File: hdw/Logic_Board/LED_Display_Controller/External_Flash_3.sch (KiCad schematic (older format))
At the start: 16 parts, among them U2001 SST25PF020B

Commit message: Added some digikey partnumbers to components
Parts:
- C2001: footprint (none) -> Capacitors_SMD:C_0603; Digi-Key PN PN -> 311-1344-1-ND; Voltage 25V -> 50V
- C2002: Digi-Key PN PN -> 1276-1921-1-ND; Voltage 25V -> 50V
- C2003: Digi-Key PN PN -> 1276-1018-1-ND; Voltage 25V -> 50V
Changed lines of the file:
@@
 F 0 "C2001" H 5815 5530 50  0000 L CNN
 F 1 "0.1uF" H 5815 5330 50  0000 L CNN
-F 2 "" H 5828 5280 50  0001 C CNN
+F 2 "Capacitors_SMD:C_0603" H 5828 5280 50  0001 C CNN
 F 3 "" H 5815 5530 50  0001 C CNN
 F 4 "0603" H 5640 5530 50  0000 R CNN "display_footprint"
-F 5 "25V" H 5640 5430 50  0000 R CNN "Voltage"
+F 5 "50V" H 5640 5430 50  0000 R CNN "Voltage"
 F 6 "X7R" H 5640 5330 50  0000 R CNN "Dielectric"
-F 7 "PN" H 6215 5930 60  0001 C CNN "Digi-Key PN"
+F 7 "311-1344-1-ND" H 6215 5930 60  0001 C CNN "Digi-Key PN"
 	1    5790 5430
 	1    0    0    -1
@@
 F 3 "" H 6115 5530 50  0001 C CNN
 F 4 "0603" H 5940 5530 50  0001 R CNN "display_footprint"
-F 5 "25V" H 5940 5430 50  0001 R CNN "Voltage"
+F 5 "50V" H 5940 5430 50  0001 R CNN "Voltage"
 F 6 "X7R" H 5940 5330 50  0001 R CNN "Dielectric"
-F 7 "PN" H 6515 5930 60  0001 C CNN "Digi-Key PN"
+F 7 "1276-1921-1-ND" H 6515 5930 60  0001 C CNN "Digi-Key PN"
 	1    6090 5430
 	1    0    0    -1
@@
 F 3 "" H 6415 5530 50  0001 C CNN
 F 4 "0603" H 6240 5530 50  0001 R CNN "display_footprint"
-F 5 "25V" H 6240 5430 50  0001 R CNN "Voltage"
+F 5 "50V" H 6240 5430 50  0001 R CNN "Voltage"
 F 6 "X7R" H 6240 5330 50  0001 R CNN "Dielectric"
-F 7 "PN" H 6815 5930 60  0001 C CNN "Digi-Key PN"
+F 7 "1276-1018-1-ND" H 6815 5930 60  0001 C CNN "Digi-Key PN"
 	1    6390 5430
 	1    0    0    -1

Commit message: Finished first pass of digikey part numbers
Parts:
- R2001, R2002, R2003, R2004, R2005, R2012: Digi-Key PN PN -> A106047CT-ND
- R2006, R2007, R2008, R2009, R2010, R2011: Digi-Key PN PN -> RMCF0603FT10K0CT-ND
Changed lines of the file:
@@
 F 5 "1%" H 5410 4320 50  0000 L CNN "Tolerance"
 F 6 "1/10W" H 5410 4240 50  0000 L CNN "Wattage"
-F 7 "PN" H 5630 4720 60  0001 C CNN "Digi-Key PN"
+F 7 "RMCF0603FT10K0CT-ND" H 5630 4720 60  0001 C CNN "Digi-Key PN"
 	1    5330 4320
 	1    0    0    -1
@@
 F 5 "1%" H 4600 4320 50  0000 L CNN "Tolerance"
 F 6 "1/10W" H 4600 4240 50  0000 L CNN "Wattage"
-F 7 "PN" H 4820 4720 60  0001 C CNN "Digi-Key PN"
+F 7 "RMCF0603FT10K0CT-ND" H 4820 4720 60  0001 C CNN "Digi-Key PN"
 	1    4520 4320
 	1    0    0    -1
@@
 F 5 "1%" H 5190 3130 50  0000 L CNN "Tolerance"
 F 6 "1/10W" H 5190 3050 50  0000 L CNN "Wattage"
-F 7 "PN" H 5410 3530 60  0001 C CNN "Digi-Key PN"
+F 7 "RMCF0603FT10K0CT-ND" H 5410 3530 60  0001 C CNN "Digi-Key PN"
 	1    5110 3130
 	1    0    0    -1
@@
 F 5 "1%" H 4600 3130 50  0000 L CNN "Tolerance"
 F 6 "1/10W" H 4600 3050 50  0000 L CNN "Wattage"
-F 7 "PN" H 4820 3530 60  0001 C CNN "Digi-Key PN"
+F 7 "RMCF0603FT10K0CT-ND" H 4820 3530 60  0001 C CNN "Digi-Key PN"
 	1    4520 3130
 	1    0    0    -1
@@
 F 5 "1%" H 4010 3130 50  0000 L CNN "Tolerance"
 F 6 "1/10W" H 4010 3050 50  0000 L CNN "Wattage"
-F 7 "PN" H 4230 3530 60  0001 C CNN "Digi-Key PN"
+F 7 "RMCF0603FT10K0CT-ND" H 4230 3530 60  0001 C CNN "Digi-Key PN"
 	1    3930 3130
 	1    0    0    -1
@@
 F 5 "1%" H 6830 3850 50  0000 L CNN "Tolerance"
 F 6 "1/10W" H 6830 3770 50  0000 L CNN "Wattage"
-F 7 "PN" H 7050 4250 60  0001 C CNN "Digi-Key PN"
+F 7 "RMCF0603FT10K0CT-ND" H 7050 4250 60  0001 C CNN "Digi-Key PN"
 	1    6750 3850
 	1    0    0    -1
@@
 F 5 "1%" V 3620 3450 50  0001 C CNN "Tolerance"
 F 6 "1/10W" V 3720 3450 50  0001 C CNN "Wattage"
-F 7 "PN" H 3720 3850 60  0001 C CNN "Digi-Key PN"
+F 7 "A106047CT-ND" H 3720 3850 60  0001 C CNN "Digi-Key PN"
 	1    3420 3450
 	0    1    1    0
@@
 F 5 "1%" V 7330 3450 50  0001 C CNN "Tolerance"
 F 6 "1/10W" V 7430 3450 50  0001 C CNN "Wattage"
-F 7 "PN" H 7430 3850 60  0001 C CNN "Digi-Key PN"
+F 7 "A106047CT-ND" H 7430 3850 60  0001 C CNN "Digi-Key PN"
 	1    7130 3450
 	0    1    1    0
@@
 F 5 "1%" V 3620 3550 50  0001 C CNN "Tolerance"
 F 6 "1/10W" V 3720 3550 50  0001 C CNN "Wattage"
-F 7 "PN" H 3720 3950 60  0001 C CNN "Digi-Key PN"
+F 7 "A106047CT-ND" H 3720 3950 60  0001 C CNN "Digi-Key PN"
 	1    3420 3550
 	0    1    1    0
@@
 F 5 "1%" V 3620 3750 50  0001 C CNN "Tolerance"
 F 6 "1/10W" V 3720 3750 50  0001 C CNN "Wattage"
-F 7 "PN" H 3720 4150 60  0001 C CNN "Digi-Key PN"
+F 7 "A106047CT-ND" H 3720 4150 60  0001 C CNN "Digi-Key PN"
 	1    3420 3750
 	0    1    1    0
@@
 F 5 "1%" V 3620 3850 50  0001 C CNN "Tolerance"
 F 6 "1/10W" V 3720 3850 50  0001 C CNN "Wattage"
-F 7 "PN" H 3720 4250 60  0001 C CNN "Digi-Key PN"
+F 7 "A106047CT-ND" H 3720 4250 60  0001 C CNN "Digi-Key PN"
 	1    3420 3850
 	0    1    1    0
@@
 F 5 "1%" V 3620 3650 50  0001 C CNN "Tolerance"
 F 6 "1/10W" V 3720 3650 50  0001 C CNN "Wattage"
-F 7 "PN" H 3720 4050 60  0001 C CNN "Digi-Key PN"
+F 7 "A106047CT-ND" H 3720 4050 60  0001 C CNN "Digi-Key PN"
 	1    3420 3650
 	0    1    1    0

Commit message: First pass assignment of footprints to all components
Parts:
- C2002, C2003: footprint (none) -> Capacitors_SMD:C_0603
- R2001, R2002, R2003, R2004, R2005, R2006, R2007, R2008, R2009, R2010, R2011, R2012: footprint (none) -> Resistors_SMD:R_0603
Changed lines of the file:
@@
 F 0 "R2010" H 5270 4320 50  0000 R CNN
 F 1 "10k" V 5330 4320 50  0000 C CNN
-F 2 "" H 5330 4320 50  0001 C CNN
+F 2 "Resistors_SMD:R_0603" H 5330 4320 50  0001 C CNN
 F 3 "" H 5330 4320 50  0001 C CNN
 F 4 "0603" H 5410 4400 50  0000 L CNN "display_footprint"
@@
 F 0 "R2008" H 4460 4320 50  0000 R CNN
 F 1 "10k" V 4520 4320 50  0000 C CNN
-F 2 "" H 4520 4320 50  0001 C CNN
+F 2 "Resistors_SMD:R_0603" H 4520 4320 50  0001 C CNN
 F 3 "" H 4520 4320 50  0001 C CNN
 F 4 "0603" H 4600 4400 50  0000 L CNN "display_footprint"
@@
 F 0 "R2009" H 5050 3130 50  0000 R CNN
 F 1 "10k" V 5110 3130 50  0000 C CNN
-F 2 "" H 5110 3130 50  0001 C CNN
+F 2 "Resistors_SMD:R_0603" H 5110 3130 50  0001 C CNN
 F 3 "" H 5110 3130 50  0001 C CNN
 F 4 "0603" H 5190 3210 50  0000 L CNN "display_footprint"
@@
 F 0 "R2007" H 4460 3130 50  0000 R CNN
 F 1 "10k" V 4520 3130 50  0000 C CNN
-F 2 "" H 4520 3130 50  0001 C CNN
+F 2 "Resistors_SMD:R_0603" H 4520 3130 50  0001 C CNN
 F 3 "" H 4520 3130 50  0001 C CNN
 F 4 "0603" H 4600 3210 50  0000 L CNN "display_footprint"
@@
 F 0 "R2006" H 3870 3130 50  0000 R CNN
 F 1 "10k" V 3930 3130 50  0000 C CNN
-F 2 "" H 3930 3130 50  0001 C CNN
+F 2 "Resistors_SMD:R_0603" H 3930 3130 50  0001 C CNN
 F 3 "" H 3930 3130 50  0001 C CNN
 F 4 "0603" H 4010 3210 50  0000 L CNN "display_footprint"
@@
 F 0 "R2011" H 6690 3850 50  0000 R CNN
 F 1 "10k" V 6750 3850 50  0000 C CNN
-F 2 "" H 6750 3850 50  0001 C CNN
+F 2 "Resistors_SMD:R_0603" H 6750 3850 50  0001 C CNN
 F 3 "" H 6750 3850 50  0001 C CNN
 F 4 "0603" H 6830 3930 50  0000 L CNN "display_footprint"
@@
 F 0 "R2001" V 3380 3580 50  0000 L CNN
 F 1 "100" V 3420 3450 50  0000 C CNN
-F 2 "" H 3420 3450 50  0001 C CNN
+F 2 "Resistors_SMD:R_0603" H 3420 3450 50  0001 C CNN
 F 3 "" H 3420 3450 50  0001 C CNN
 F 4 "0603" V 3520 3450 50  0001 C CNN "display_footprint"
@@
 F 0 "R2012" V 7030 3450 50  0000 C CNN
 F 1 "100" V 7130 3450 50  0000 C CNN
-F 2 "" H 7130 3450 50  0001 C CNN
+F 2 "Resistors_SMD:R_0603" H 7130 3450 50  0001 C CNN
 F 3 "" H 7130 3450 50  0001 C CNN
 F 4 "0603" V 7230 3450 50  0001 C CNN "display_footprint"
@@
 F 0 "C2002" H 6115 5530 50  0000 L CNN
 F 1 "10nF" H 6115 5330 50  0000 L CNN
-F 2 "" H 6128 5280 50  0001 C CNN
+F 2 "Capacitors_SMD:C_0603" H 6128 5280 50  0001 C CNN
 F 3 "" H 6115 5530 50  0001 C CNN
 F 4 "0603" H 5940 5530 50  0001 R CNN "display_footprint"
@@
 F 0 "C2003" H 6415 5530 50  0000 L CNN
 F 1 "1nF" H 6415 5330 50  0000 L CNN
-F 2 "" H 6428 5280 50  0001 C CNN
+F 2 "Capacitors_SMD:C_0603" H 6428 5280 50  0001 C CNN
 F 3 "" H 6415 5530 50  0001 C CNN
 F 4 "0603" H 6240 5530 50  0001 R CNN "display_footprint"
@@
 F 0 "R2002" V 3380 3680 50  0000 L CNN
 F 1 "100" V 3420 3550 50  0000 C CNN
-F 2 "" H 3420 3550 50  0001 C CNN
+F 2 "Resistors_SMD:R_0603" H 3420 3550 50  0001 C CNN
 F 3 "" H 3420 3550 50  0001 C CNN
 F 4 "0603" V 3520 3550 50  0001 C CNN "display_footprint"
@@
 F 0 "R2004" V 3380 3880 50  0000 L CNN
 F 1 "100" V 3420 3750 50  0000 C CNN
-F 2 "" H 3420 3750 50  0001 C CNN
+F 2 "Resistors_SMD:R_0603" H 3420 3750 50  0001 C CNN
 F 3 "" H 3420 3750 50  0001 C CNN
 F 4 "0603" V 3520 3750 50  0001 C CNN "display_footprint"
@@
 F 0 "R2005" V 3380 3980 50  0000 L CNN
 F 1 "100" V 3420 3850 50  0000 C CNN
-F 2 "" H 3420 3850 50  0001 C CNN
+F 2 "Resistors_SMD:R_0603" H 3420 3850 50  0001 C CNN
 F 3 "" H 3420 3850 50  0001 C CNN
 F 4 "0603" V 3520 3850 50  0001 C CNN "display_footprint"
@@
 F 0 "R2003" V 3380 3780 50  0000 L CNN
 F 1 "100" V 3420 3650 50  0000 C CNN
-F 2 "" H 3420 3650 50  0001 C CNN
+F 2 "Resistors_SMD:R_0603" H 3420 3650 50  0001 C CNN
 F 3 "" H 3420 3650 50  0001 C CNN
 F 4 "0603" V 3520 3650 50  0001 C CNN "display_footprint"

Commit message: Resolved a few library dependencies
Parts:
- R2001, R2002, R2003, R2004, R2005, R2006, R2007, R2008, R2009, R2010, R2011, R2012: symbol Custom_Library:R_Custom -> LED_Display_Local_Library:R_Custom
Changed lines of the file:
@@
 $EndComp
 $Comp
-L Custom_Library:R_Custom R2010
+L LED_Display_Local_Library:R_Custom R2010
 U 1 1 5BBE8125
 P 5330 4320
@@
 $EndComp
 $Comp
-L Custom_Library:R_Custom R2008
+L LED_Display_Local_Library:R_Custom R2008
 U 1 1 5BBE8130
 P 4520 4320
@@
 $EndComp
 $Comp
-L Custom_Library:R_Custom R2009
+L LED_Display_Local_Library:R_Custom R2009
 U 1 1 5BBE813B
 P 5110 3130
@@
 $EndComp
 $Comp
-L Custom_Library:R_Custom R2007
+L LED_Display_Local_Library:R_Custom R2007
 U 1 1 5BBE8146
 P 4520 3130
@@
 $EndComp
 $Comp
-L Custom_Library:R_Custom R2006
+L LED_Display_Local_Library:R_Custom R2006
 U 1 1 5BBE8151
 P 3930 3130
@@
 $EndComp
 $Comp
-L Custom_Library:R_Custom R2011
+L LED_Display_Local_Library:R_Custom R2011
 U 1 1 5BBE815C
 P 6750 3850
@@
 $EndComp
 $Comp
-L Custom_Library:R_Custom R2001
+L LED_Display_Local_Library:R_Custom R2001
 U 1 1 5BBE818B
 P 3420 3450
@@
 FLASH_SCK
 $Comp
-L Custom_Library:R_Custom R2012
+L LED_Display_Local_Library:R_Custom R2012
 U 1 1 5BBE81B8
 P 7130 3450
@@
 	6090 5240 6390 5240
 $Comp
-L Custom_Library:R_Custom R2002
+L LED_Display_Local_Library:R_Custom R2002
 U 1 1 5BBE8203
 P 3420 3550
@@
 $EndComp
 $Comp
-L Custom_Library:R_Custom R2004
+L LED_Display_Local_Library:R_Custom R2004
 U 1 1 5BBE820E
 P 3420 3750
@@
 $EndComp
 $Comp
-L Custom_Library:R_Custom R2005
+L LED_Display_Local_Library:R_Custom R2005
 U 1 1 5BBE8219
 P 3420 3850
@@
 ~FLASH_Hold
 $Comp
-L Custom_Library:R_Custom R2003
+L LED_Display_Local_Library:R_Custom R2003
 U 1 1 5BC1CF11
 P 3420 3650

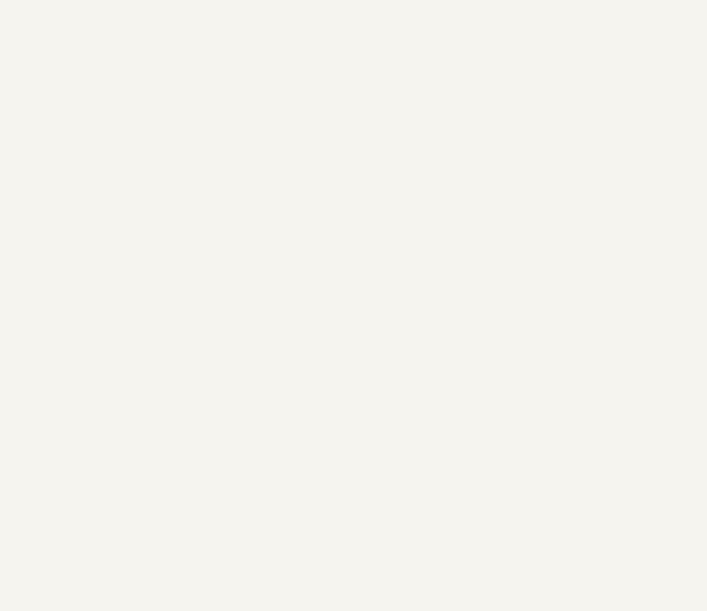
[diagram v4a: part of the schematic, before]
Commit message: Added flash chip select LEDs
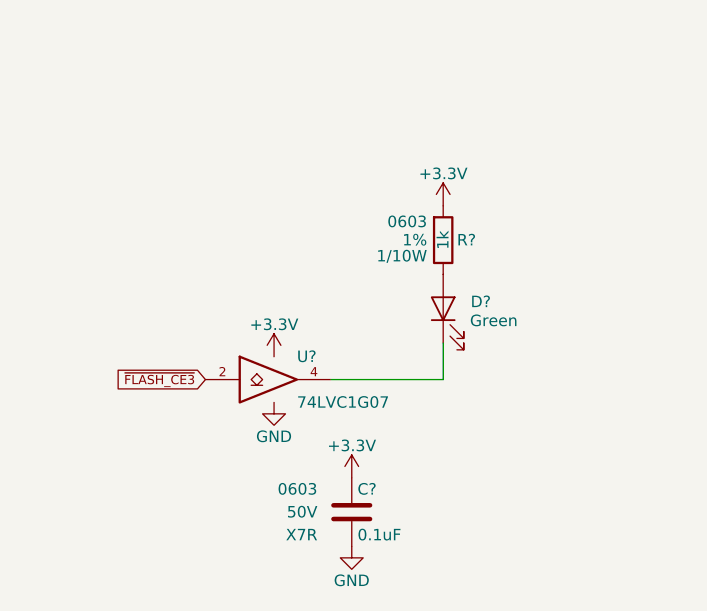
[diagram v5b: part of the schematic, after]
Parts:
- added C?: 0.1uF, Capacitors_SMD:C_0603, symbol LED_Display_Local_Library:C_Custom
- added D?: Green, LEDs:LED_0603, symbol Device:LED
- added R?: 1k, Resistors_SMD:R_0603, symbol LED_Display_Local_Library:R_Custom
- added U?: 74LVC1G07, TO_SOT_Packages_SMD:SOT-353_SC-70-5, symbol LED_Display_Local_Library:74LVC1G07_Power
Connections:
- net +3V3: now also C?.1, R?.1, U?.5 (VCC)
- net GND: now also C?.2, U?.3 (GND)
- net ~FLASH_CE3: now also U?.2
- new net: D?.1 (K), U?.4
- new net: D?.2 (A), R?.2
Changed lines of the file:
@@
 Wire Wire Line
 	4520 3850 5680 3850
+$Comp
+L LED_Display_Local_Library:C_Custom C?
+U 1 1 5C171D48
+P 2010 6900
+AR Path="/5BAAE16C/5C171D48" Ref="C?"  Part="1"
+AR Path="/5BB181D8/5C171D48" Ref="C?"  Part="1"
+AR Path="/5BB2595E/5C171D48" Ref="C?"  Part="1"
+AR Path="/5BB25AEA/5C171D48" Ref="C?"  Part="1"
+F 0 "C?" H 2035 7000 50  0000 L CNN
+F 1 "0.1uF" H 2035 6800 50  0000 L CNN
+F 2 "Capacitors_SMD:C_0603" H 2048 6750 50  0001 C CNN
+F 3 "" H 2035 7000 50  0001 C CNN
+F 4 "0603" H 1860 7000 50  0000 R CNN "display_footprint"
+F 5 "50V" H 1860 6900 50  0000 R CNN "Voltage"
+F 6 "X7R" H 1860 6800 50  0000 R CNN "Dielectric"
+F 7 "311-1344-1-ND" H 2435 7400 60  0001 C CNN "Digi-Key PN"
+	1    2010 6900
+	1    0    0    -1
+$EndComp
+$Comp
+L LED_Display_Local_Library:74LVC1G07_Power U?
+U 1 1 5C171D50
+P 1670 6320
+AR Path="/5BB2595E/5C171D50" Ref="U?"  Part="1"
+AR Path="/5BB25AEA/5C171D50" Ref="U?"  Part="1"
+F 0 "U?" H 1770 6420 50  0000 L CNN
+F 1 "74LVC1G07" H 1770 6220 50  0000 L CNN
+F 2 "TO_SOT_Packages_SMD:SOT-353_SC-70-5" H 1670 6320 50  0001 C CNN
+F 3 "http://www.ti.com/lit/sg/scyt129e/scyt129e.pdf" H 1670 6320 50  0001 C CNN
+F 4 "296-8486-1-ND" H 1670 6320 50  0001 C CNN "Digi-Key PN"
+	1    1670 6320
+	1    0    0    -1
+$EndComp
+$Comp
+L power:+3.3V #PWR?
+U 1 1 5C171D57
+P 1670 6220
+AR Path="/5BB2595E/5C171D57" Ref="#PWR?"  Part="1"
+AR Path="/5BB25AEA/5C171D57" Ref="#PWR?"  Part="1"
+F 0 "#PWR?" H 1670 6070 50  0001 C CNN
+F 1 "+3.3V" H 1670 6360 50  0000 C CNN
+F 2 "" H 1670 6220 50  0001 C CNN
+F 3 "" H 1670 6220 50  0001 C CNN
+	1    1670 6220
+	1    0    0    -1
+$EndComp
+$Comp
+L power:+3.3V #PWR?
+U 1 1 5C171D5D
+P 2010 6750
+AR Path="/5BB2595E/5C171D5D" Ref="#PWR?"  Part="1"
+AR Path="/5BB25AEA/5C171D5D" Ref="#PWR?"  Part="1"
+F 0 "#PWR?" H 2010 6600 50  0001 C CNN
+F 1 "+3.3V" H 2010 6890 50  0000 C CNN
+F 2 "" H 2010 6750 50  0001 C CNN
+F 3 "" H 2010 6750 50  0001 C CNN
+	1    2010 6750
+	1    0    0    -1
+$EndComp
+$Comp
+L power:GND #PWR?
+U 1 1 5C171D63
+P 2010 7050
+AR Path="/5BB2595E/5C171D63" Ref="#PWR?"  Part="1"
+AR Path="/5BB25AEA/5C171D63" Ref="#PWR?"  Part="1"
+F 0 "#PWR?" H 2010 6800 50  0001 C CNN
+F 1 "GND" H 2010 6900 50  0000 C CNN
+F 2 "" H 2010 7050 50  0001 C CNN
+F 3 "" H 2010 7050 50  0001 C CNN
+	1    2010 7050
+	1    0    0    -1
+$EndComp
+$Comp
+L power:GND #PWR?
+U 1 1 5C171D69
+P 1670 6420
+AR Path="/5BB2595E/5C171D69" Ref="#PWR?"  Part="1"
+AR Path="/5BB25AEA/5C171D69" Ref="#PWR?"  Part="1"
+F 0 "#PWR?" H 1670 6170 50  0001 C CNN
+F 1 "GND" H 1670 6270 50  0000 C CNN
+F 2 "" H 1670 6420 50  0001 C CNN
+F 3 "" H 1670 6420 50  0001 C CNN
+	1    1670 6420
+	1    0    0    -1
+$EndComp
+Text GLabel 1370 6320 0    40   Input ~ 0
+~FLASH_CE3
+$Comp
+L power:+3.3V #PWR?
+U 1 1 5C171D70
+P 2410 5560
+AR Path="/5BB844FD/5C171D70" Ref="#PWR?"  Part="1"
+AR Path="/5BF346B3/5C171D70" Ref="#PWR?"  Part="1"
+AR Path="/5BB2595E/5C171D70" Ref="#PWR?"  Part="1"
+AR Path="/5BB25AEA/5C171D70" Ref="#PWR?"  Part="1"
+F 0 "#PWR?" H 2410 5410 50  0001 C CNN
+F 1 "+3.3V" H 2410 5700 50  0000 C CNN
+F 2 "" H 2410 5560 50  0001 C CNN
+F 3 "" H 2410 5560 50  0001 C CNN
+	1    2410 5560
+	1    0    0    -1
+$EndComp
+Wire Wire Line
+	1920 6320 2410 6320
+Wire Wire Line
+	2410 6320 2410 6160
+$Comp
+L LED_Display_Local_Library:R_Custom R?
+U 1 1 5C171D7C
+P 2410 5710
+AR Path="/5BAAE1F3/5C171D7C" Ref="R?"  Part="1"
+AR Path="/5BAAE1DC/5C171D7C" Ref="R?"  Part="1"
+AR Path="/5BAAE16C/5C171D7C" Ref="R?"  Part="1"
+AR Path="/5BB844FD/5C171D7C" Ref="R?"  Part="1"
+AR Path="/5BF346B3/5C171D7C" Ref="R?"  Part="1"
+AR Path="/5BB2595E/5C171D7C" Ref="R?"  Part="1"
+AR Path="/5BB25AEA/5C171D7C" Ref="R?"  Part="1"
+F 0 "R?" H 2350 5710 50  0000 R CNN
+F 1 "1k" V 2410 5710 50  0000 C CNN
+F 2 "Resistors_SMD:R_0603" H 2410 5710 50  0001 C CNN
+F 3 "" H 2410 5710 50  0001 C CNN
+F 4 "0603" H 2480 5790 50  0000 L CNN "display_footprint"
+F 5 "1%" H 2480 5710 50  0000 L CNN "Tolerance"
+F 6 "1/10W" H 2480 5640 50  0000 L CNN "Wattage"
+F 7 "RMCF0603FT1K00CT-ND" H 2710 6110 60  0001 C CNN "Digi-Key PN"
+	1    2410 5710
+	-1   0    0    -1
+$EndComp
+$Comp
+L Device:LED D?
+U 1 1 5C171D84
+P 2410 6010
+AR Path="/5BB844FD/5C171D84" Ref="D?"  Part="1"
+AR Path="/5BF346B3/5C171D84" Ref="D?"  Part="1"
+AR Path="/5BB2595E/5C171D84" Ref="D?"  Part="1"
+AR Path="/5BB25AEA/5C171D84" Ref="D?"  Part="1"
+F 0 "D?" V 2440 5890 50  0000 R CNN
+F 1 "Green" V 2357 5893 50  0000 R CNN
+F 2 "LEDs:LED_0603" H 2410 6010 50  0001 C CNN
+F 3 "~" H 2410 6010 50  0001 C CNN
+F 4 "160-1446-1-ND" H -2600 3010 50  0001 C CNN "Digi-Key PN"
+	1    2410 6010
+	0    -1   -1   0
+$EndComp
 $EndSCHEMATC

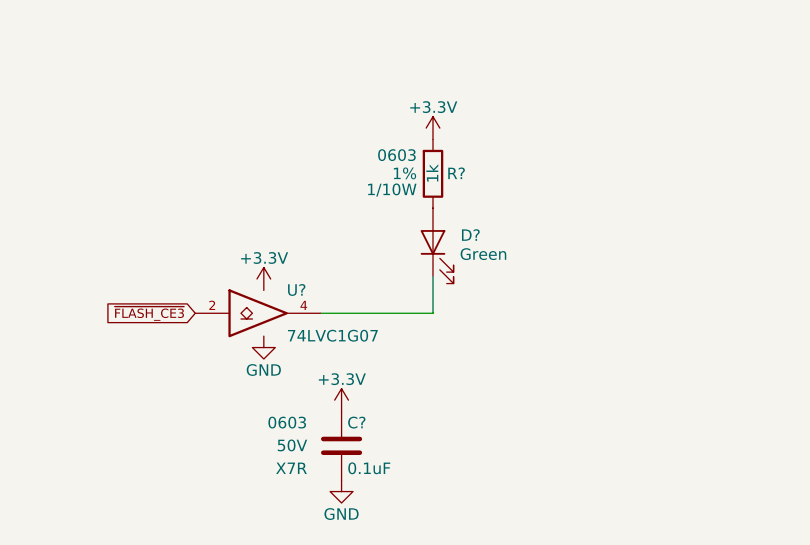
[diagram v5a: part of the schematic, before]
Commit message: Added WIFI comm LED
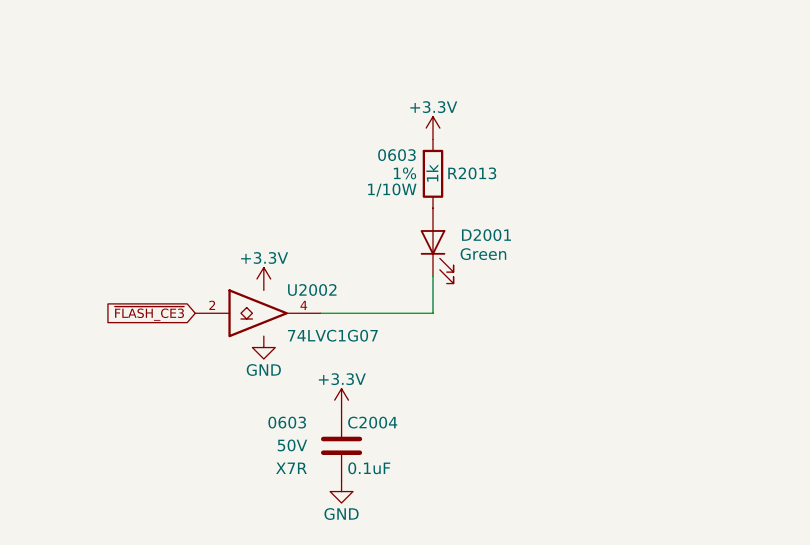
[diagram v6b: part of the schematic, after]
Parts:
- gave numbers to parts that had none: 4
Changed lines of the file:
@@
 AR Path="/5BB181D8/5C171D48" Ref="C?"  Part="1"
 AR Path="/5BB2595E/5C171D48" Ref="C?"  Part="1"
-AR Path="/5BB25AEA/5C171D48" Ref="C?"  Part="1"
-F 0 "C?" H 2035 7000 50  0000 L CNN
+AR Path="/5BB25AEA/5C171D48" Ref="C2004"  Part="1"
+F 0 "C2004" H 2035 7000 50  0000 L CNN
 F 1 "0.1uF" H 2035 6800 50  0000 L CNN
 F 2 "Capacitors_SMD:C_0603" H 2048 6750 50  0001 C CNN
@@
 P 1670 6320
 AR Path="/5BB2595E/5C171D50" Ref="U?"  Part="1"
-AR Path="/5BB25AEA/5C171D50" Ref="U?"  Part="1"
-F 0 "U?" H 1770 6420 50  0000 L CNN
+AR Path="/5BB25AEA/5C171D50" Ref="U2002"  Part="1"
+F 0 "U2002" H 1770 6420 50  0000 L CNN
 F 1 "74LVC1G07" H 1770 6220 50  0000 L CNN
 F 2 "TO_SOT_Packages_SMD:SOT-353_SC-70-5" H 1670 6320 50  0001 C CNN
@@
 P 1670 6220
 AR Path="/5BB2595E/5C171D57" Ref="#PWR?"  Part="1"
-AR Path="/5BB25AEA/5C171D57" Ref="#PWR?"  Part="1"
-F 0 "#PWR?" H 1670 6070 50  0001 C CNN
+AR Path="/5BB25AEA/5C171D57" Ref="#PWR02011"  Part="1"
+F 0 "#PWR02011" H 1670 6070 50  0001 C CNN
 F 1 "+3.3V" H 1670 6360 50  0000 C CNN
 F 2 "" H 1670 6220 50  0001 C CNN
@@
 P 2010 6750
 AR Path="/5BB2595E/5C171D5D" Ref="#PWR?"  Part="1"
-AR Path="/5BB25AEA/5C171D5D" Ref="#PWR?"  Part="1"
-F 0 "#PWR?" H 2010 6600 50  0001 C CNN
+AR Path="/5BB25AEA/5C171D5D" Ref="#PWR02013"  Part="1"
+F 0 "#PWR02013" H 2010 6600 50  0001 C CNN
 F 1 "+3.3V" H 2010 6890 50  0000 C CNN
 F 2 "" H 2010 6750 50  0001 C CNN
@@
 P 2010 7050
 AR Path="/5BB2595E/5C171D63" Ref="#PWR?"  Part="1"
-AR Path="/5BB25AEA/5C171D63" Ref="#PWR?"  Part="1"
-F 0 "#PWR?" H 2010 6800 50  0001 C CNN
+AR Path="/5BB25AEA/5C171D63" Ref="#PWR02014"  Part="1"
+F 0 "#PWR02014" H 2010 6800 50  0001 C CNN
 F 1 "GND" H 2010 6900 50  0000 C CNN
 F 2 "" H 2010 7050 50  0001 C CNN
@@
 P 1670 6420
 AR Path="/5BB2595E/5C171D69" Ref="#PWR?"  Part="1"
-AR Path="/5BB25AEA/5C171D69" Ref="#PWR?"  Part="1"
-F 0 "#PWR?" H 1670 6170 50  0001 C CNN
+AR Path="/5BB25AEA/5C171D69" Ref="#PWR02012"  Part="1"
+F 0 "#PWR02012" H 1670 6170 50  0001 C CNN
 F 1 "GND" H 1670 6270 50  0000 C CNN
 F 2 "" H 1670 6420 50  0001 C CNN
@@
 AR Path="/5BF346B3/5C171D70" Ref="#PWR?"  Part="1"
 AR Path="/5BB2595E/5C171D70" Ref="#PWR?"  Part="1"
-AR Path="/5BB25AEA/5C171D70" Ref="#PWR?"  Part="1"
-F 0 "#PWR?" H 2410 5410 50  0001 C CNN
+AR Path="/5BB25AEA/5C171D70" Ref="#PWR02015"  Part="1"
+F 0 "#PWR02015" H 2410 5410 50  0001 C CNN
 F 1 "+3.3V" H 2410 5700 50  0000 C CNN
 F 2 "" H 2410 5560 50  0001 C CNN
@@
 AR Path="/5BF346B3/5C171D7C" Ref="R?"  Part="1"
 AR Path="/5BB2595E/5C171D7C" Ref="R?"  Part="1"
-AR Path="/5BB25AEA/5C171D7C" Ref="R?"  Part="1"
-F 0 "R?" H 2350 5710 50  0000 R CNN
+AR Path="/5BB25AEA/5C171D7C" Ref="R2013"  Part="1"
+F 0 "R2013" H 2350 5710 50  0000 R CNN
 F 1 "1k" V 2410 5710 50  0000 C CNN
 F 2 "Resistors_SMD:R_0603" H 2410 5710 50  0001 C CNN
@@
 AR Path="/5BF346B3/5C171D84" Ref="D?"  Part="1"
 AR Path="/5BB2595E/5C171D84" Ref="D?"  Part="1"
-AR Path="/5BB25AEA/5C171D84" Ref="D?"  Part="1"
-F 0 "D?" V 2440 5890 50  0000 R CNN
+AR Path="/5BB25AEA/5C171D84" Ref="D2001"  Part="1"
+F 0 "D2001" V 2440 5890 50  0000 R CNN
 F 1 "Green" V 2357 5893 50  0000 R CNN
 F 2 "LEDs:LED_0603" H 2410 6010 50  0001 C CNN
